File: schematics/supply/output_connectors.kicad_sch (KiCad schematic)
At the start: 38 parts, among them J20 Conn_01x05_Pin, J21 banana jack + fuse 15A, J22 banana jack + fuse 15A, J23 Conn_01x05_Pin, J24 Conn_01x02_Pin, J25 Conn_01x02_Pin, J26 Conn_02x04_Odd_Even, J27 jst xh angle, J28 jst xh angle, Q12 IRLML0030, Q13 IRLML0030, Q4 IRF7425PbF, U26 TP4056, U27 INA3221

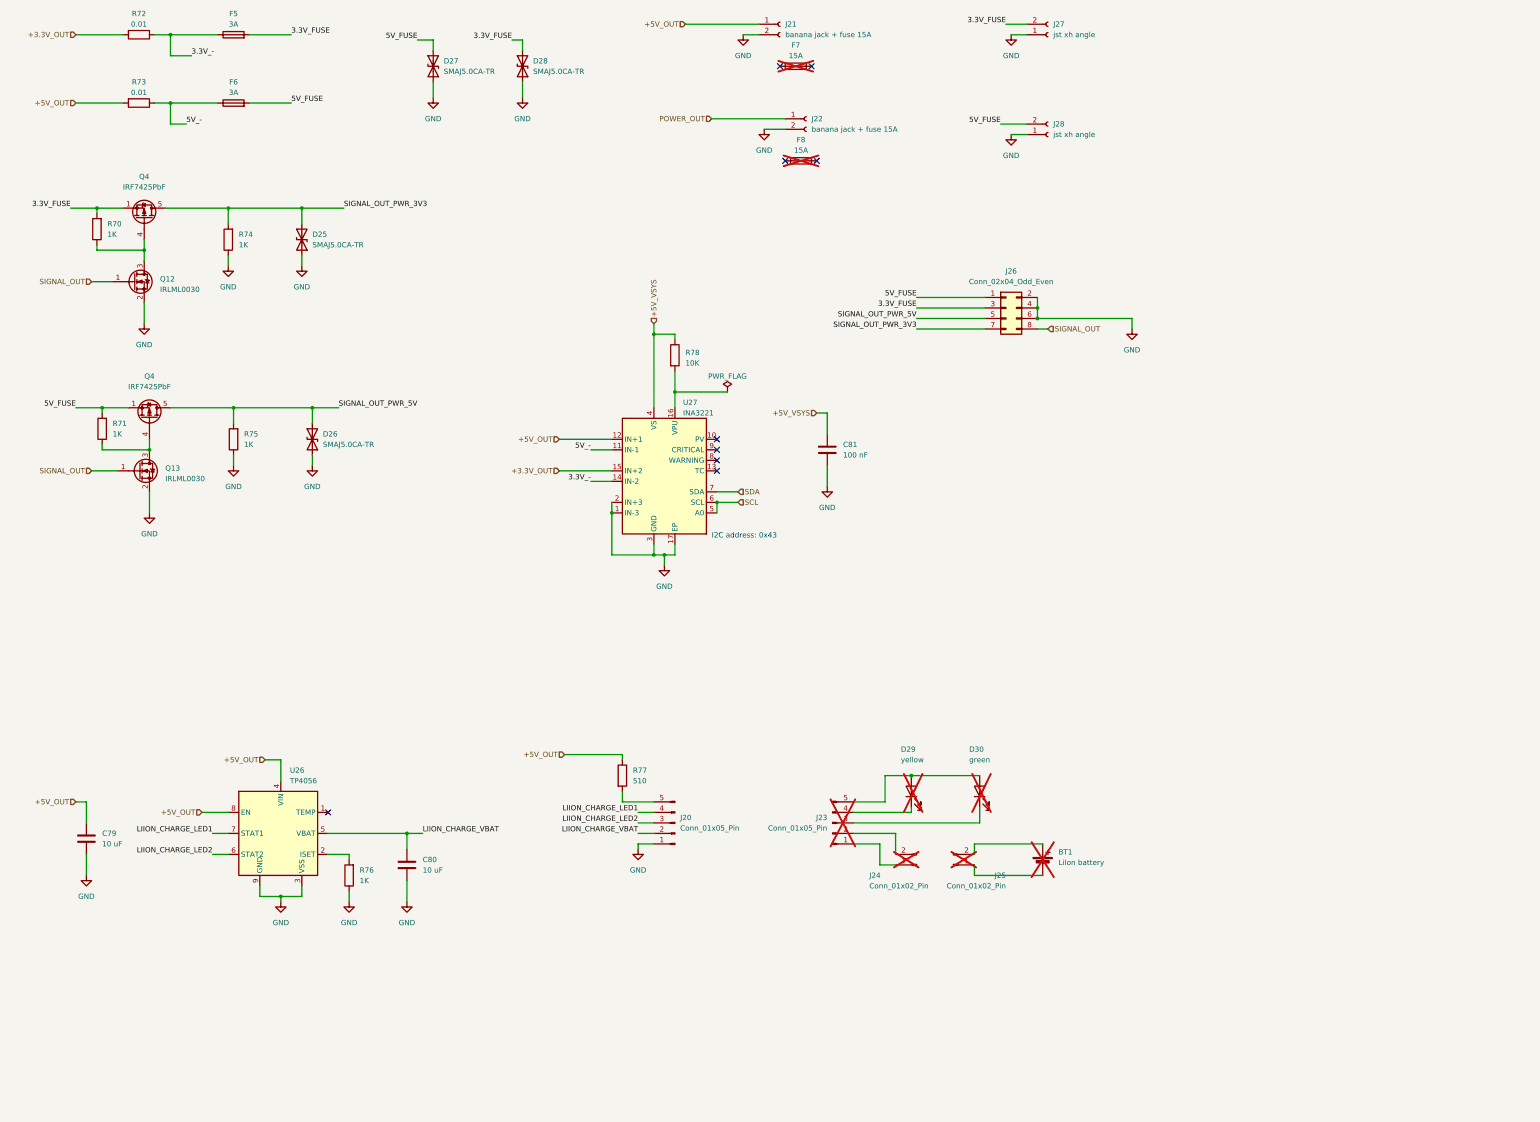
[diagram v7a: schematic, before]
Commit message: Board#1 schematics rewrited
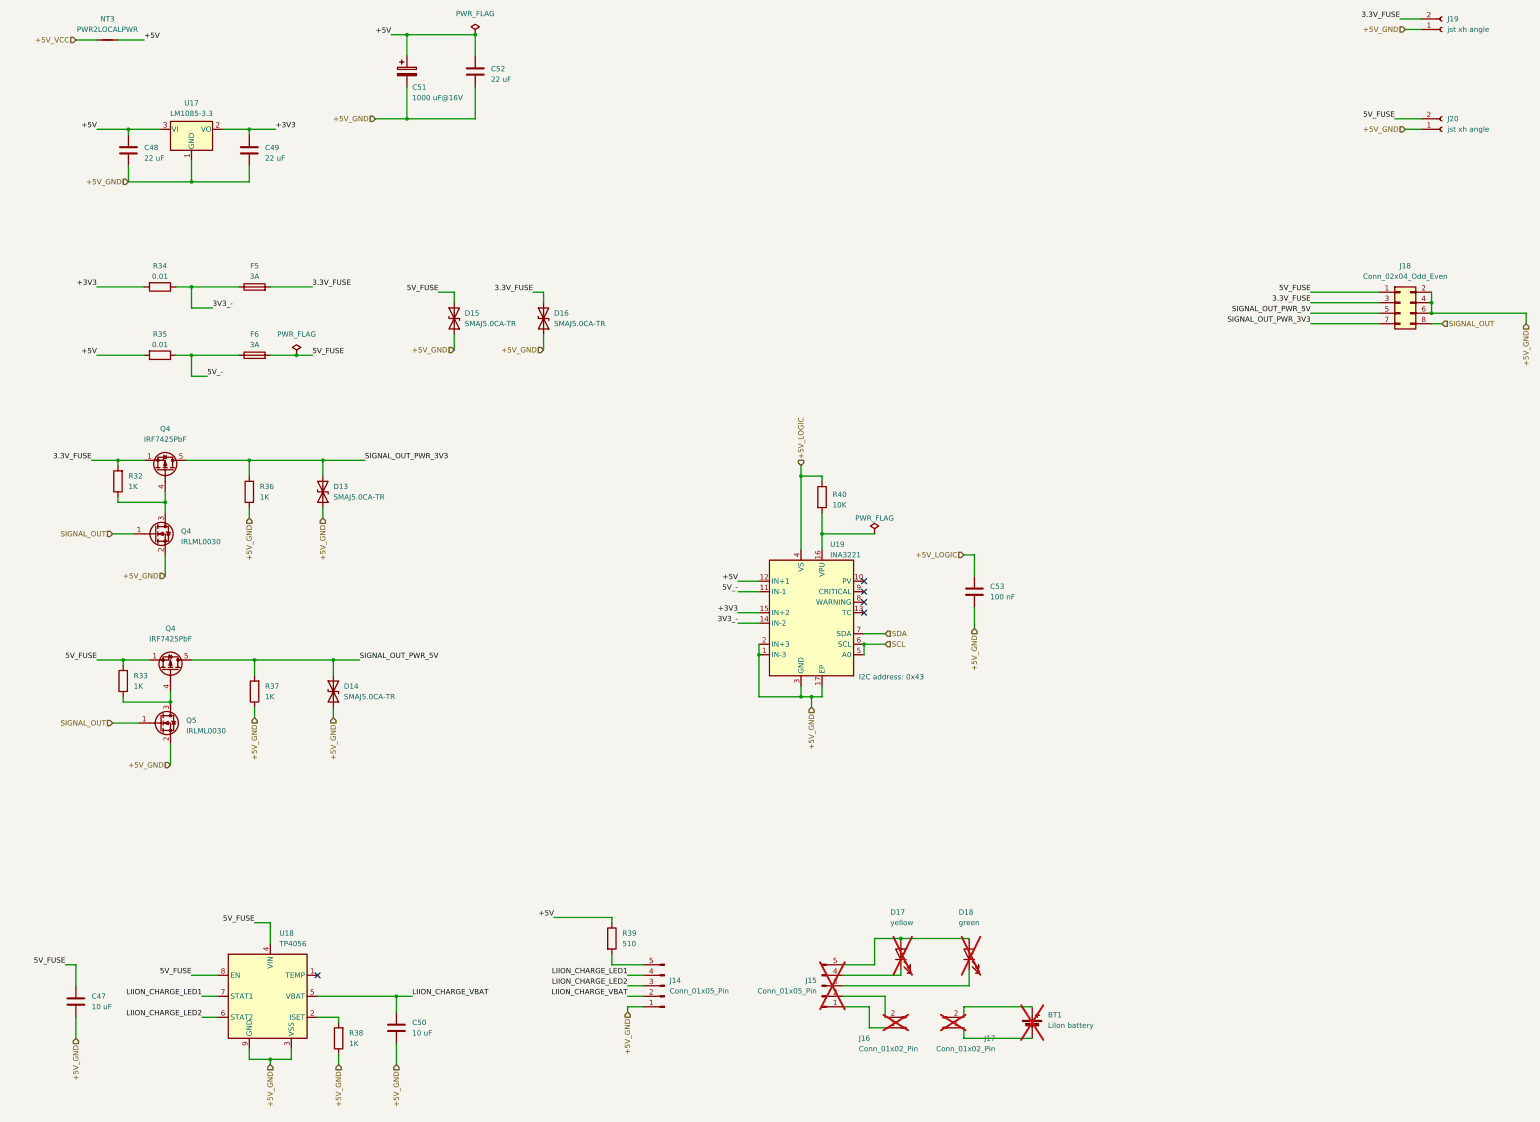
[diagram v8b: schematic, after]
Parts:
- removed F7, F8: 15A, symbol Device:Fuse
- removed J21, J22: banana jack + fuse 15A, Connector_Wire:SolderWire-1.5sqmm_1x02_P6mm_D1.7mm_OD3mm, symbol Connector:Conn_01x02_Socket
- added C48, C49, C52: 22 uF, Capacitor_SMD:C_1210_3225Metric, symbol Device:C
- added C51: 1000 uF@16V, Capacitor_THT:CP_Radial_D10.0mm_P5.00mm, symbol Device:C_Polarized
- added NT3: PWR2LOCALPWR, NetTie:NetTie-2_SMD_Pad0.5mm, symbol Device:NetTie_2
- added U17: LM1085-3.3, Package_TO_SOT_SMD:TO-263-3_TabPin2, symbol Regulator_Linear:LM1085-3.3
- renumbered C79 to C47, C80 to C50, C81 to C53, D25 to D13, D26 to D14, D27 to D15, D28 to D16, D29 to D17, D30 to D18, J20 to J14, J23 to J15, J24 to J16, J25 to J17, J26 to J18, J27 to J19, J28 to J20, Q12 to Q4, Q13 to Q5, R70 to R32, R71 to R33, R72 to R34, R73 to R35, R74 to R36, R75 to R37, R76 to R38, R77 to R39, R78 to R40, U26 to U18, U27 to U19
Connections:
- net 5V_FUSE: now also C47.2, U18.4 (VIN), U18.8 (EN)
- net +3.3V_OUT renamed +3V3
- net +3V3: now also C49.2, U17.2 (VO)
- net +5V_OUT renamed +5V
- net +5V: now also C48.2, C51.1, C52.2, NT3.2, U17.3 (VI); no longer C47.2, U18.4 (VIN), U18.8 (EN)
- net +5V_VSYS renamed +5V_LOGIC
- net 3.3V_- renamed 3V3_-
- net GND renamed +5V_GND
- net +5V_GND: now also C48.1, C49.1, C51.2, C52.1, U17.1 (GND)
- new net +5V_VCC: NT3.1
- no-connect marks 9 -> 5
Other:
- moved on the sheet: BT1, C47, C50, C53, D13, D14, D15, D16, D17, D18, F5, F6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
